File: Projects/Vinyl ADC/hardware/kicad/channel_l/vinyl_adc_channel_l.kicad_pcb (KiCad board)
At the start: 2 copper layers, 100 x 100 mm, 43 parts, among them J20 LINE IN L, J21 Q SEL, J7 2x8 BUS, U20 TL072, U21 LM311, U22 TL072, U23 74HC74, U24 74HC04

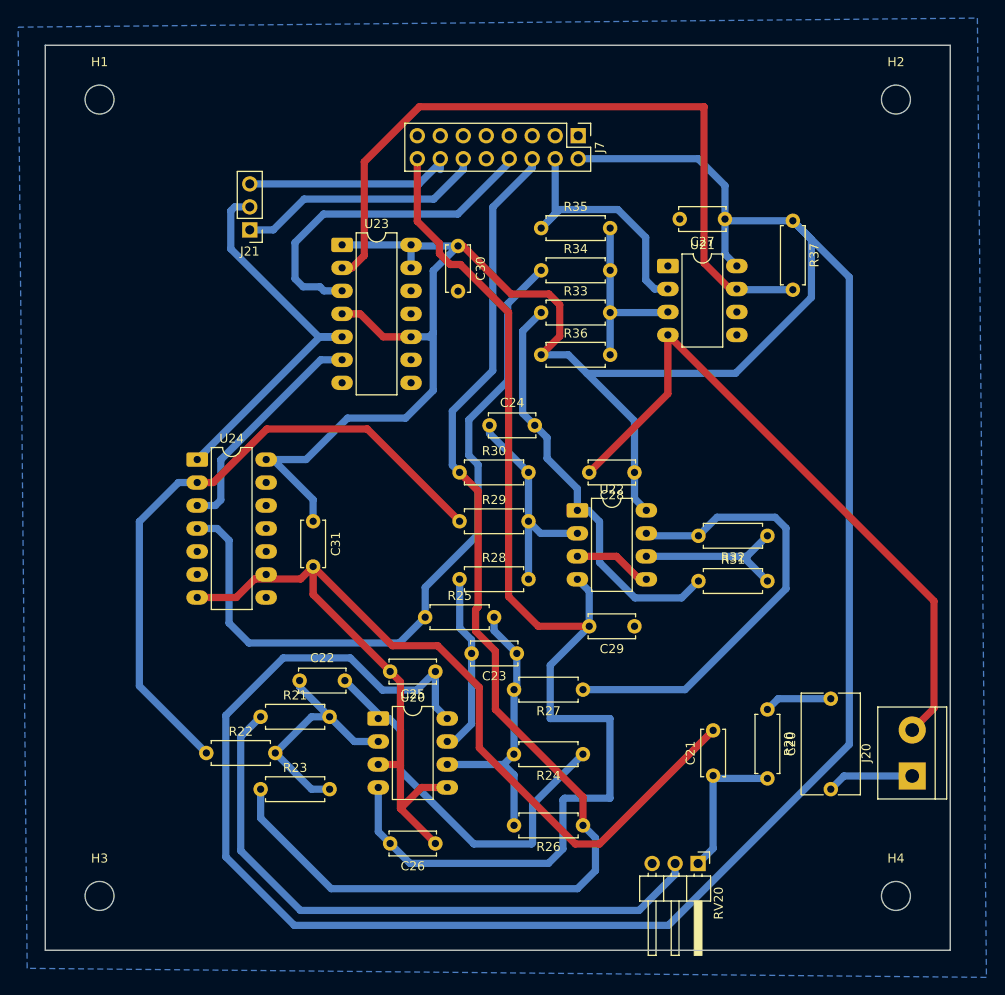
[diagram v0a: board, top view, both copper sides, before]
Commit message: Vinyl ADC: cut the channel double-sided, restore the DRC rules
The three boards were unjudgeable: a previous rebuild deleted every
.kicad_dru, so all three reported bare clearance errors with no way to
tell a real one from the documented exception. Restore them per the
memberOfFootprint recipe -- all 116 hits turn out to be intra-footprint
pad-to-pad at 0.840 mm against the 0.85 mm rule, on fixed 2.54 mm header
pitch, and not one of them was real. The rules do override the board
minimum in KiCad 10; checked rather than assumed.

Netclass was 0.5/0.6 on all three, below the boards' own 0.85/0.8 minima,
so anything that routed them would have laid copper the mill cannot cut.

The channel artwork is now DOUBLE-SIDED -- it is the one milled twice, and
it gets the two pieces of double-sided stock. Its ground was genuinely
broken before this: 32 GND pads in two electrically separate pieces, 30
pour fragments, 24 pads that could only get home through a track, and nine
wire bridges. That fault would have shipped twice. It is now one whole
plane, no stranded pads, zero vias, and one link left.

Four architectures were measured on the same placement before picking one:

  signals on top, GND plane below   6 links, 0 vias, plane whole    91 top joints
  both layers, GND poured           2 links, 1 via,  plane in 3     55 top joints
  leftovers on top  <- shipped      1 link,  0 vias, plane whole    20 top joints

An open link is a wire, and a wire is soldered at both ends -- the same two
joints a milled top-side trace between those pads needs. So moving only the
leftovers to the top costs nothing to build and removes the wire. The full
re-routes buy a prettier plane for 35-71 extra joints, most under sockets.

Registration for the flip is already in the artwork: the four M3 holes sit
at exactly +/-44.00 mm from the board centre in both axes, so the pattern
maps onto itself and two dowels through a diagonal pair are enough.

digital was not routed at all -- 3 of 20 nets, zone u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
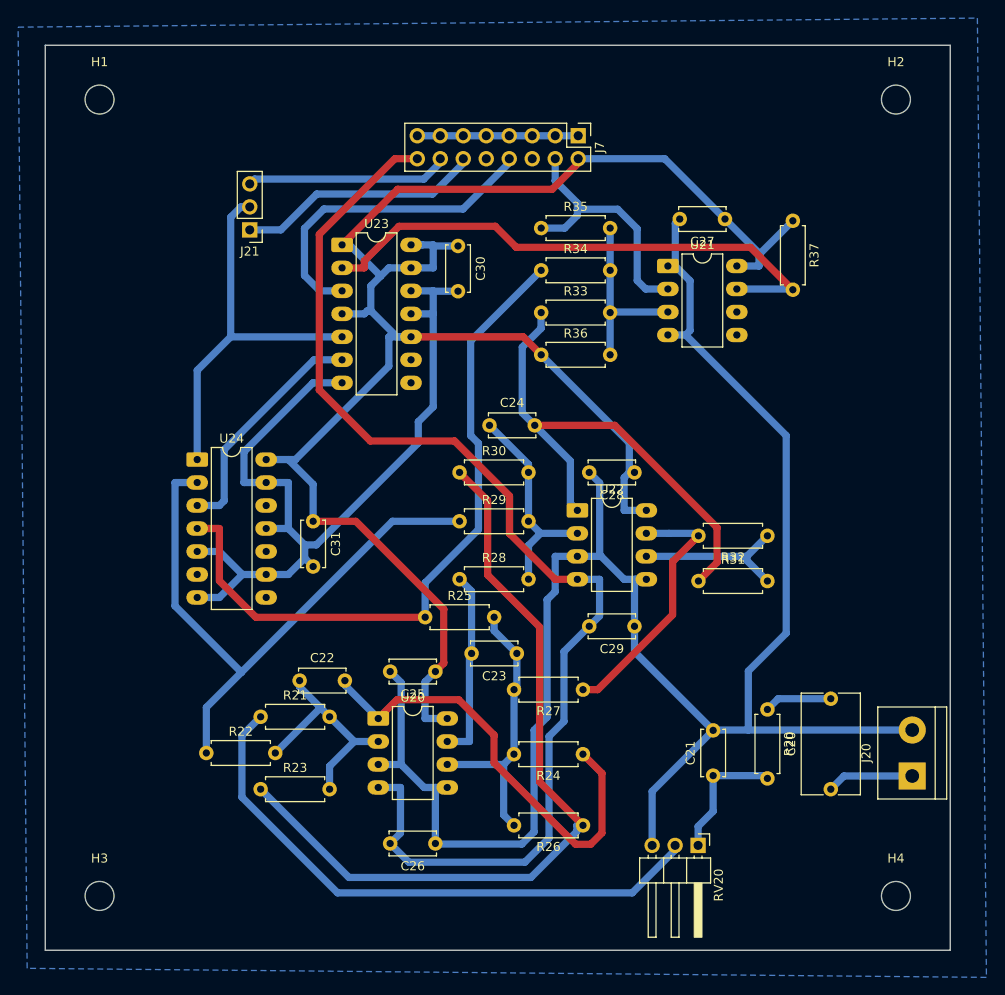
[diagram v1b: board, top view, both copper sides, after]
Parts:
- moved RV20 2.00 mm to (92.1, 108.4)
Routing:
- net +5V: track 383.3 -> 200.0 mm
- net GND: track 209.4 -> 328.9 mm
- net VREF_N: track 133.4 -> 87.1 mm
- net Net-(R27-Pad1): track 51.4 -> 29.1 mm
- net CMP_L: track 81.7 -> 61.3 mm
- net Net-(C24-Pad2): track 46.0 -> 56.8 mm
- net Net-(C22-Pad2): track 43.3 -> 49.8 mm
- net Net-(R21-Pad1): track 69.3 -> 64.5 mm
- net DACN_L: track 72.5 -> 68.0 mm
- net DACP_L: track 81.5 -> 77.0 mm
- net Net-(C21-Pad1): track 16.5 -> 14.5 mm
- net Net-(U20A--): track 27.2 -> 25.4 mm
- net MCLK: track 37.9 -> 36.1 mm
- net -5V: track 134.7 -> 133.1 mm
- net Q_OUT: track 44.4 -> 43.2 mm
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
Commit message: Vinyl ADC: channel artwork finished, and its production set
VREF_N to J7 pin 6 is routed -- the one link FreeRouting would not close
at 30 or 100 passes with the whole top layer free. The channel board is
now 26/26 nets in one piece, both oracles agreeing at 0 unconnected, 0
vias, 0 stranded pads.

Its ground pour was in ten pieces: the GND zone had island removal set to
Never, leaving nine floating fragments of 1.2 to 12.9 mm2, none carrying
a pad, all reported as isolated_copper. Set to Always and refilled. Pour
is one piece, those nine DRC violations are gone, and nothing depended on
them -- zero stranded pads before and after. DRC now reports nothing but
thirteen silk_overlap.

The schematic moved on the page by a uniform +19.05, +57.15 mm. Netlist
unchanged: check_split still accounts for all 92 nets and 377 nodes, and
check_fixture still passes.

One thing worth knowing that is NOT in the acceptance bar: cutspan reads
1.141 board diagonals against 0.725 for the automated route. The ground
return detours 161 mm further than the straight line and the worst point
is J7 pin 1, the bus GND pin. Not a fault, does not block the mill, but
this artwork is cut twice and feeds a modulator whose noise floor is
ground-dependent.

The production set is versioned here rather than ignored, against the
policy in production/.gitignore, because it has to be reachable from the
CAM machine and that machine has no KiCad. It is committed alongside the
exact board it came from, so it is not the stale set that policy exists
to prevent. Regenerate rather than edit it.

export_production.ps1 could not write the gerbers: it passes
-o "$OutDir\gerbers\", and the trailing backslash before the closing
quote is read as an escaped quote, so the path ran on and came back as
personal-projects\ADC\... -- kicad-cli then reported the board missing.
Invisible unless the path has a space in it, and "Vinyl ADC" has one. The
DXF steps pass a full filename and were fine. Gerbers and drill exported
by h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
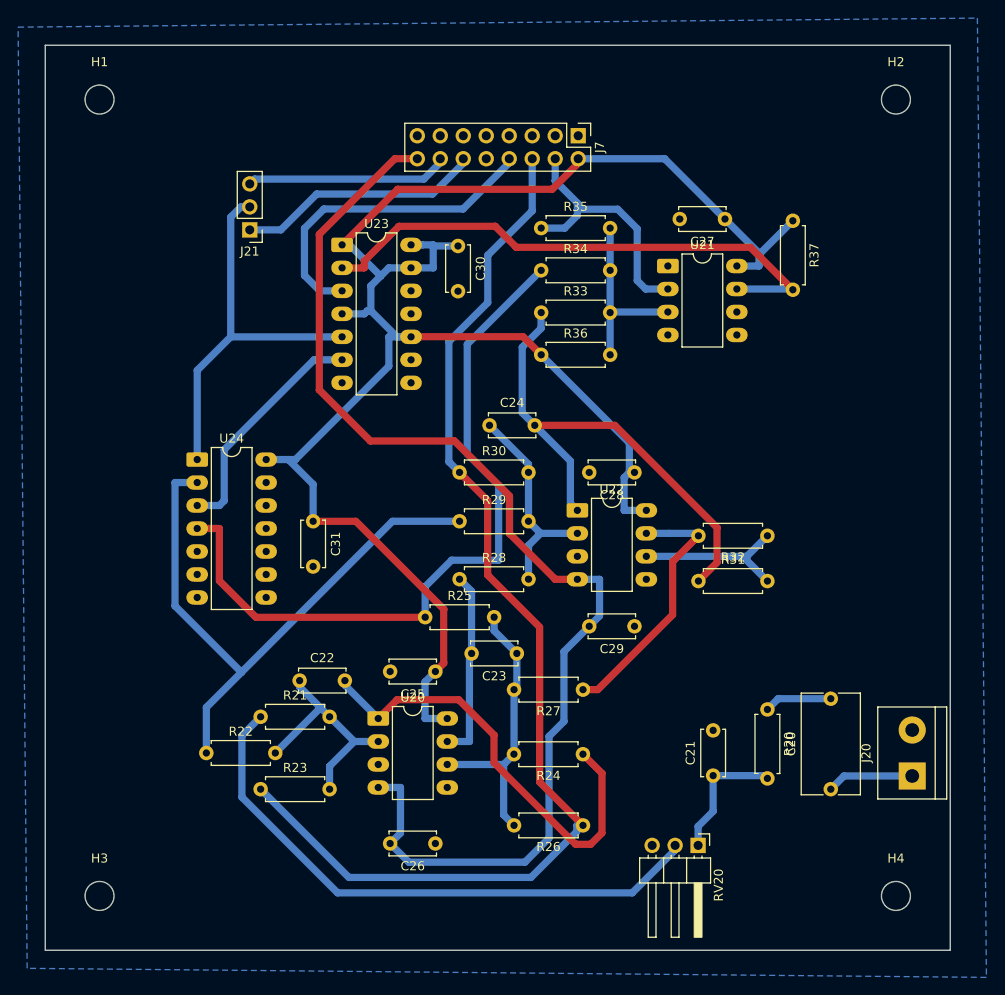
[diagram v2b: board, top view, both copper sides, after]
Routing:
- net GND: track 328.9 -> 0.00 mm
- net VREF_N: track 87.1 -> 126.1 mm
- net DACP_L: track 77.0 -> 82.2 mm
